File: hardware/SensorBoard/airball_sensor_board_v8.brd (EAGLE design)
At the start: 5.6 x 9.2 mm, 61 parts, among them IC1 CP2102, J2 USB Female Type C Connector, T1 BC846, T2 BC846, U1 BQ24075, U2 BQ27441-G1, U3 BMP388, U4 ESP-WROOM-32, U7 SP0503BAHT

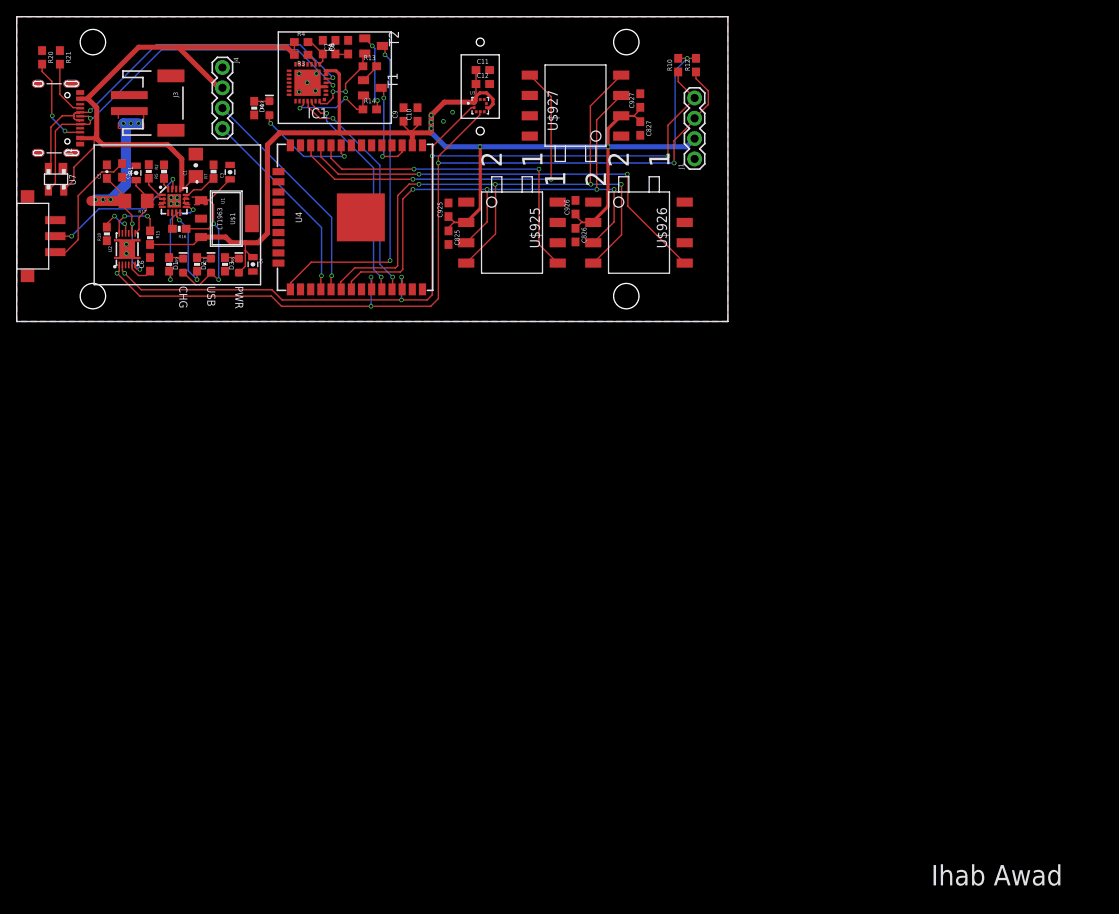
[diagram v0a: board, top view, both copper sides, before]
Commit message: Formatting
Added titles and formatting to schematic and board.
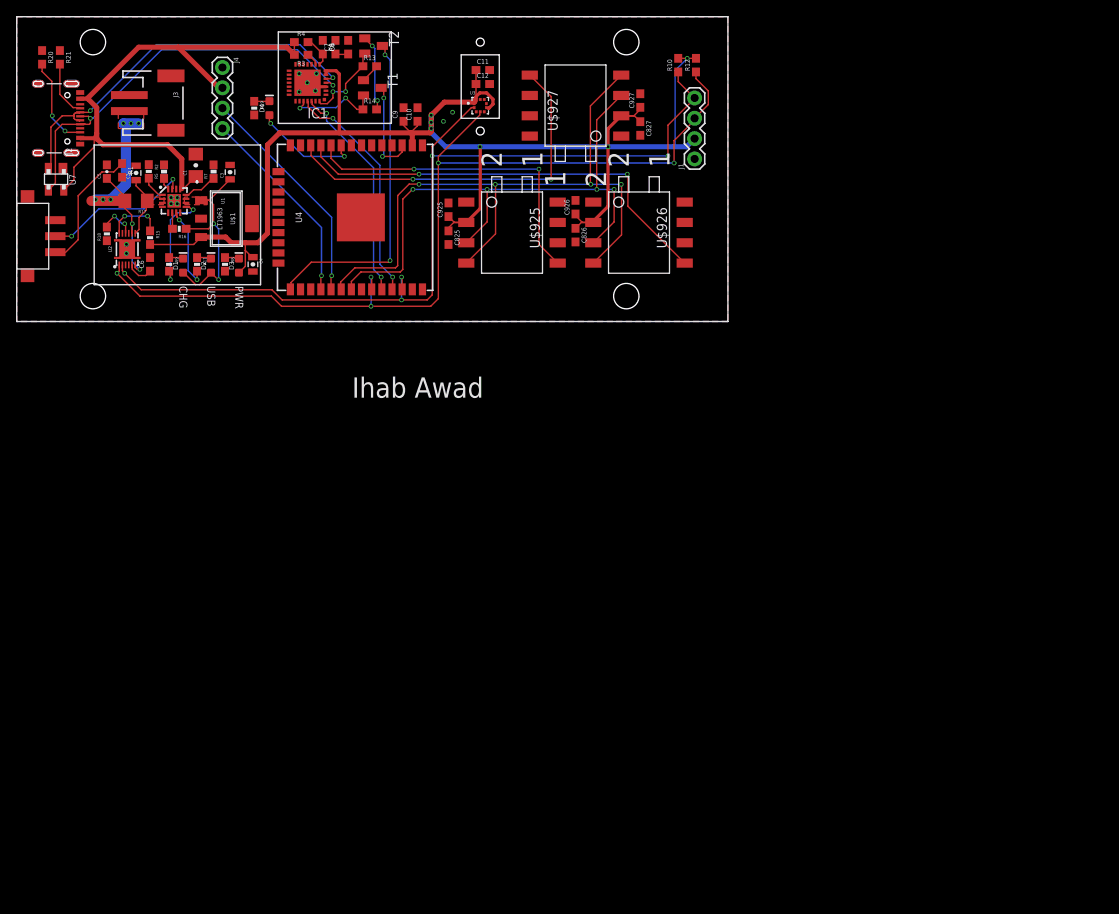
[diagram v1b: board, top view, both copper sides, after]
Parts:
- moved FRAME1 70.5 mm to (11.0, -8.70)
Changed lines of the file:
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@@
 <dimension x1="0" y1="0" x2="3.81" y2="8.89" x3="-7.62" y3="4.445" textsize="0.8128" textratio="15" layer="47" dtype="vertical" unit="inch"/>
 <dimension x1="0" y1="0" x2="1.27" y2="11.43" x3="0.635" y3="-1.397" textsize="0.8128" textratio="15" layer="47" dtype="horizontal" unit="inch"/>
-<text x="114.3" y="-70.485" size="2.54" layer="21">Ihab Awad</text>
+<text x="41.91" y="-9.525" size="2.54" layer="21">Ihab Awad</text>
 <wire x1="9.68375" y1="22.06625" x2="30.48" y2="22.06625" width="0.1778" layer="21" grouprefs="POWER"/>
 <wire x1="30.48" y1="22.06625" x2="30.48" y2="4.60375" width="0.1778" layer="21" grouprefs="POWER"/>
@@
 <attribute name="VALUE" x="4.6355" y="33.02" size="0.6096" layer="27" font="vector" ratio="20" rot="R270" align="top-center"/>
 </element>
-<element name="FRAME1" library="SparkFun-Aesthetics" package="CREATIVE_COMMONS" value="FRAME-LETTER" x="6.985" y="-79.0575" smashed="yes"/>
+<element name="FRAME1" library="SparkFun-Aesthetics" package="CREATIVE_COMMONS" value="FRAME-LETTER" x="11.049" y="-8.6995" smashed="yes"/>
 <element name="J4" library="SparkFun-Connectors" package="1X04" value="" x="25.7175" y="31.75" smashed="yes" rot="R270">
 <attribute name="NAME" x="27.1145" y="33.02" size="0.6096" layer="25" font="vector" ratio="20" rot="R270"/>

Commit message: Finishing touches to the board, sent to manufacturing.
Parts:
- moved U3 1.27 mm to (57.9, 28.3)
- moved C11 0.68 mm to (58.0, 32.1)
- moved C12 0.68 mm to (58.0, 30.3)
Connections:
- net V_SUPPLY_UNREG: now also J4.2
- net V_USB: no longer J4.2
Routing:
- net V_SUPPLY_UNREG: track 25.6 -> 44.3 mm, vias 2 -> 5
- net GND: track 2.54 -> 17.1 mm, vias 3 -> 139
- net V_USB: track 72.9 -> 64.2 mm
- net V_BATT: track 7.97 -> 9.87 mm
- net SCL: track 113.9 -> 115.7 mm, vias 5 -> 4
- net BATTERY_IN: track 33.4 -> 35.0 mm
- net SYSOFF_OFF: track 14.9 -> 16.5 mm
- net SCLK: track 84.1 -> 85.4 mm
- net SDA: track 117.8 -> 118.9 mm, vias 5 -> 4
- net USB_DTR: track 10.3 -> 11.4 mm
- net USB_D+: track 51.9 -> 51.0 mm
- added copper zone on layer 1, net VCC
- added copper zone on layer 16, net VCC
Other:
- board size 5.6 x 9.2 mm -> 88.9 x 38.1 mm
- board text added: "ACT"
